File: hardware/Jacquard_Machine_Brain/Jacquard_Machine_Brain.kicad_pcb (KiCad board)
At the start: 2 copper layers, 50 x 77 mm, 38 parts, among them J1 Terminal Block, J13 Molex Micro-Fit 4pos, J15 USB_A, J16 Wurth_RJ45_LED, SW1 SW_DIP_x02, SW2 SW_MEC_5G, U1 R-78E5.0-1.0, U2 Teensy4.1, U6 AO4882

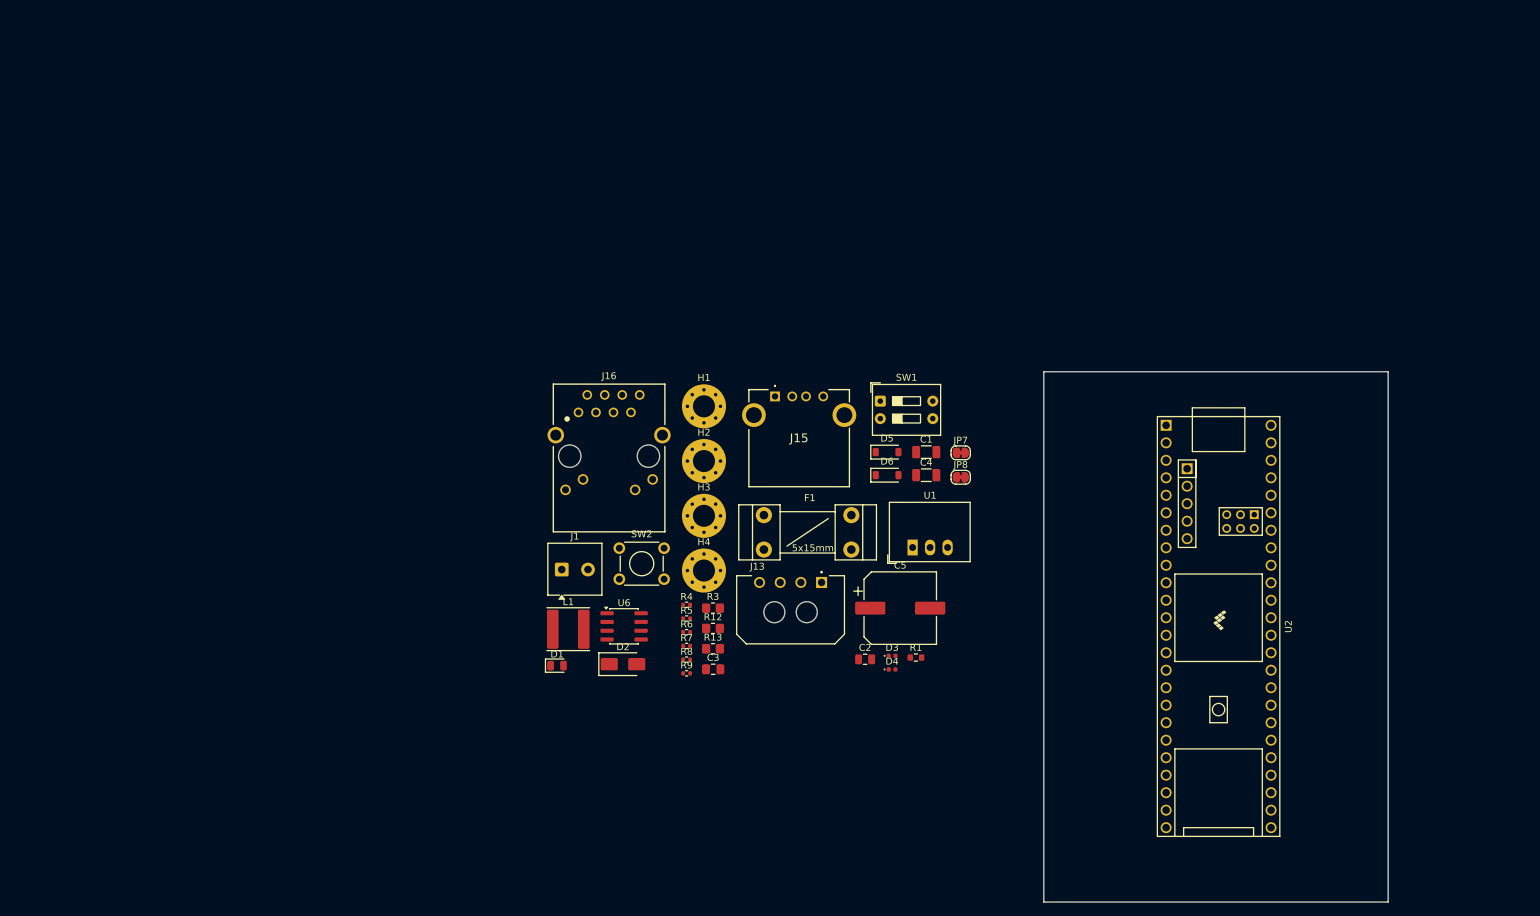
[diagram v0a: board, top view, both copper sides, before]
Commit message: Further progress on the brain
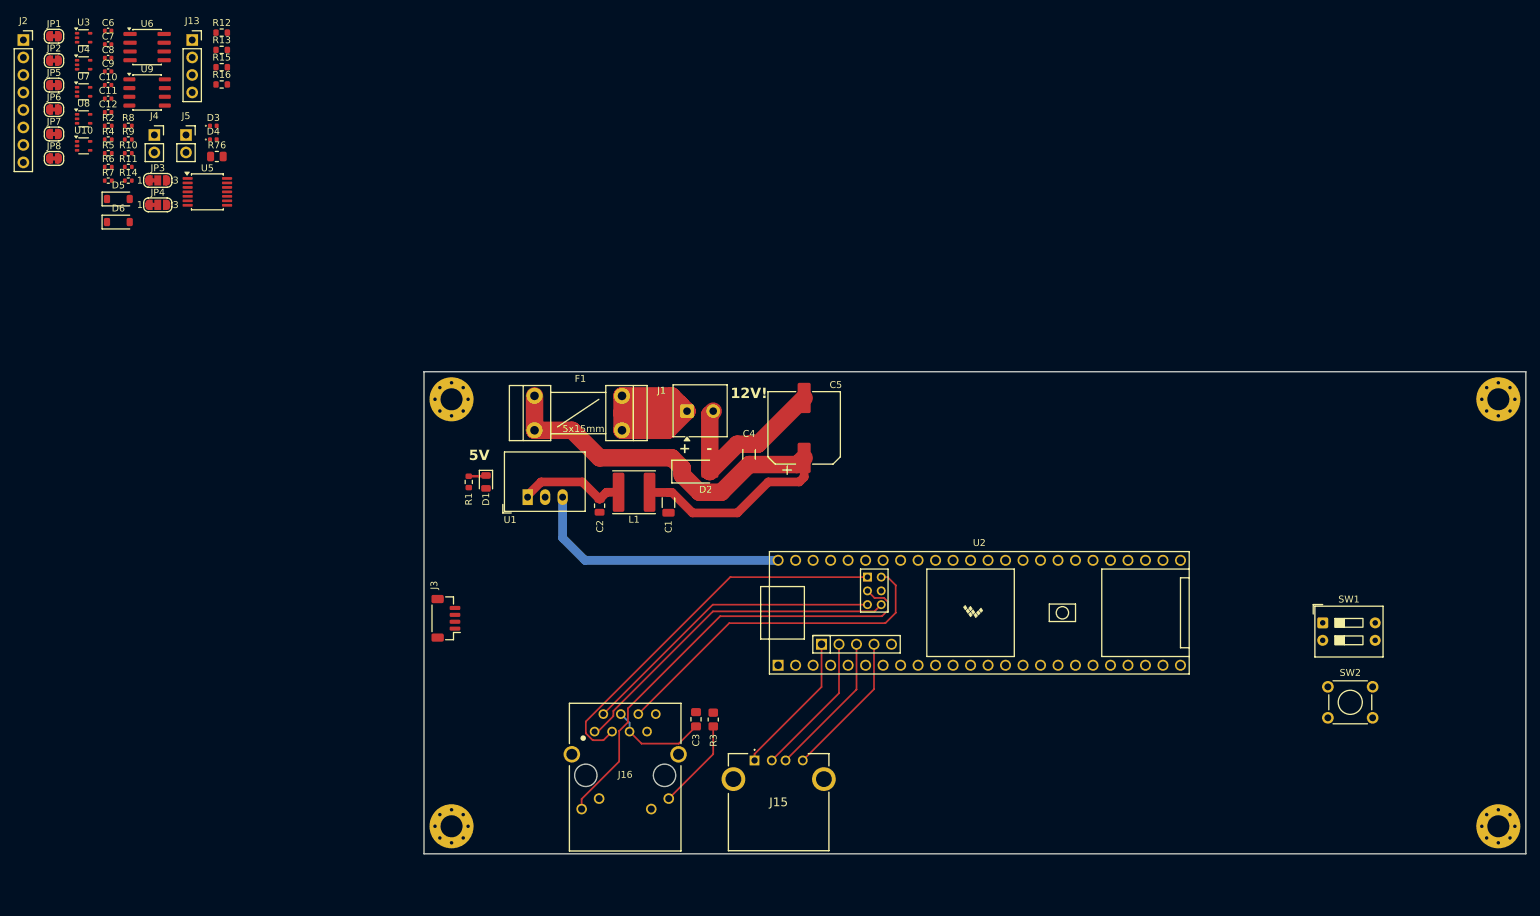
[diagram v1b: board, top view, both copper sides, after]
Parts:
- added C10: 0.1uF, Capacitor_SMD:C_0402_1005Metric, F.Cu at (14.1, 8.37)
- added C11: 0.1uF, Capacitor_SMD:C_0402_1005Metric, F.Cu at (14.1, 10.3)
- added C12: 0.1uF, Capacitor_SMD:C_0402_1005Metric, F.Cu at (14.1, 12.3)
- added C6: 0.1uF, Capacitor_SMD:C_0402_1005Metric, F.Cu at (14.1, 0.48)
- added C7: 0.1uF, Capacitor_SMD:C_0402_1005Metric, F.Cu at (14.1, 2.46)
- added C8: 0.1uF, Capacitor_SMD:C_0402_1005Metric, F.Cu at (14.1, 4.42)
- added C9: 0.1uF, Capacitor_SMD:C_0402_1005Metric, F.Cu at (14.1, 6.39)
- added J2: Conn_01x08, Connector_PinSocket_2.54mm:PinSocket_1x08_P2.54mm_Vertical, F.Cu at (1.82, 1.82)
- added J3: JST-SH 01x04, Connector_JST:JST_SH_BM04B-SRSS-TB_1x04-1MP_P1.00mm_Vertical, F.Cu at (63.2, 85.8)
- added J4: Conn_01x02, Connector_PinSocket_2.54mm:PinSocket_1x02_P2.54mm_Vertical, F.Cu at (20.8, 15.6)
- added J5: Conn_01x02, Connector_PinSocket_2.54mm:PinSocket_1x02_P2.54mm_Vertical, F.Cu at (25.4, 15.6)
- added JP1: SolderJumper_2_Bridged, Jumper:SolderJumper-2_P1.3mm_Bridged_RoundedPad1.0x1.5mm, F.Cu at (6.28, 1.27)
- added JP2: SolderJumper_2_Bridged, Jumper:SolderJumper-2_P1.3mm_Bridged_RoundedPad1.0x1.5mm, F.Cu at (6.28, 4.83)
- added JP3: SolderJumper_3_Bridged12, Jumper:SolderJumper-3_P1.3mm_Bridged12_RoundedPad1.0x1.5mm_NumberLabels, F.Cu at (21.3, 22.2)
- added JP4: SolderJumper_3_Bridged12, Jumper:SolderJumper-3_P1.3mm_Bridged12_RoundedPad1.0x1.5mm_NumberLabels, F.Cu at (21.3, 25.8)
- added JP5: SolderJumper_2_Bridged, Jumper:SolderJumper-2_P1.3mm_Bridged_RoundedPad1.0x1.5mm, F.Cu at (6.28, 8.38)
- added JP6: SolderJumper_2_Bridged, Jumper:SolderJumper-2_P1.3mm_Bridged_RoundedPad1.0x1.5mm, F.Cu at (6.28, 11.9)
- added R10: 200k, Resistor_SMD:R_0402_1005Metric, F.Cu at (17.1, 18.3)
- added R11: 100, Resistor_SMD:R_0402_1005Metric, F.Cu at (17.1, 20.3)
- added R14: 100, Resistor_SMD:R_0402_1005Metric, F.Cu at (17.1, 22.2)
- added R15: 4.7k, Resistor_SMD:R_0603_1608Metric, F.Cu at (30.6, 5.78)
- added R16: 4.7k, Resistor_SMD:R_0603_1608Metric, F.Cu at (30.6, 8.29)
- added R2: 100, Resistor_SMD:R_0402_1005Metric, F.Cu at (14.2, 14.3)
- added R76: 0Ω, Resistor_SMD:R_0805_2012Metric, F.Cu at (29.9, 18.7)
- added U10: 74AHCT1G125, Package_TO_SOT_SMD:SOT-353_SC-70-5, F.Cu at (10.6, 17.2)
- added U3: 74AHCT1G125, Package_TO_SOT_SMD:SOT-353_SC-70-5, F.Cu at (10.6, 1.50)
- added U4: 74AHCT1G125, Package_TO_SOT_SMD:SOT-353_SC-70-5, F.Cu at (10.6, 5.42)
- added U5: 74AHCT125, Package_SO:TSSOP-14_4.4x5mm_P0.65mm, F.Cu at (28.5, 23.9)
- added U7: 74AHCT1G125, Package_TO_SOT_SMD:SOT-353_SC-70-5, F.Cu at (10.6, 9.35)
- added U8: 74AHCT1G125, Package_TO_SOT_SMD:SOT-353_SC-70-5, F.Cu at (10.6, 13.3)
- added U9: PCA9306D, Package_SO:SO-8_3.9x4.9mm_P1.27mm, F.Cu at (19.8, 9.45)
- J13: value Molex Micro-Fit 4pos -> ~; footprint 0_connector:MOLEX_MICROFIT-RA-4POS_436500400 -> Connector_PinSocket_2.54mm:PinSocket_1x04_P2.54mm_Vertical
- R12, R13: value 10k -> 4.7k; footprint Resistor_SMD:R_0805_2012Metric_Pad1.20x1.40mm_HandSolder -> Resistor_SMD:R_0603_1608Metric
- moved JP7 139.6 mm to (6.28, 15.5)
- moved JP8 139.6 mm to (6.28, 19.0)
- moved D3 125.0 mm to (29.4, 14.3)
- moved D4 125.0 mm to (29.4, 16.3)
- moved H4 121.2 mm to (216.0, 116.0)
- moved J13 120.2 mm to (26.3, 1.82)
- moved D5 117.5 mm to (15.6, 24.9)
- moved D6 117.5 mm to (15.6, 28.3)
- moved H2 115.7 mm to (216.0, 54.0)
- moved R13 112.5 mm to (30.6, 3.27)
- moved R8 112.2 mm to (17.1, 14.3)
- moved R9 112.2 mm to (17.1, 16.3)
- moved R12 112.1 mm to (30.6, 0.76)
- moved U6 109.0 mm to (19.8, 2.86)
- moved R4 107.8 mm to (14.2, 16.3)
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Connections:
- net /DRAIN_1 renamed Net-(D5-A)
- net /DRAIN_2 renamed Net-(D6-A)
- D3 pad 1: LED_GND -> GND
- D4 pad 1: LED_GND -> GND
- J13 pad 3: SDA_0 -> SDA_1
- J13 pad 4: SCL_0 -> SCL_1
- JP7 pad 1: SDA_0 -> SCL_0_3.3V
- JP8 pad 1: SCL_0 -> SDA_0_3.3V
- R4 pad 1: /GATE_1 -> unconnected-(R4-Pad1)
- R5 pad 1: /GATE_2 -> unconnected-(R5-Pad1)
- U2 pad 40: SDA_0 -> SDA_0_3.3V
- U2 pad 41: SCL_0 -> SCL_0_3.3V
- U2 pad 46: unconnected-(U2-3V3-Pad46) -> +3V3
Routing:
- net +12V: track 0.00 -> 79.2 mm
- net Net-(U2-LED): track 0.00 -> 65.9 mm
- net Net-(U2-R+): track 0.00 -> 56.0 mm
- net Net-(U2-R-): track 0.00 -> 50.1 mm
- net Net-(U2-T+): track 0.00 -> 49.7 mm
- net Net-(U2-T-): track 0.00 -> 44.9 mm
- net +5V: track 0.00 -> 38.6 mm
- net Net-(J1-Pin_1): track 0.00 -> 34.9 mm
- net GNDPWR: track 0.00 -> 27.1 mm
- net GND: track 0.00 -> 21.2 mm
- net Net-(J15-D+): track 0.00 -> 21.1 mm
- net Net-(J15-D-): track 0.00 -> 20.9 mm
- net Net-(J15-VBUS): track 0.00 -> 20.9 mm
- net Net-(U1-IN): track 0.00 -> 15.7 mm
- net Net-(C3-Pad1): track 0.00 -> 14.5 mm
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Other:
- board size 50 x 77 mm -> 160 x 70 mm
- board text added: "+"
- board text added: "-"
- board text added: "12V!"
- board text added: "5V"
